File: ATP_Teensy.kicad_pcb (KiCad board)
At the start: 2 copper layers, 73 x 73 mm, 18 parts, among them J1 Screw_Terminal_01x02, U1 BMP388_3966, U2 L7805CV, U3 FT231X_XBee_USB_Adapter, U4 MPU6050, U5 Teensy4.1, U6 GPS

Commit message: Update notes on schematic
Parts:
- 9V PWR: renamed from J1
- renumbered D2 to 5V, D1 to 9V, U1 to BMP, U6 to GPS, U4 to IMU, U2 to REG, U5 to TEENSY4.1, U3 to XBEE_USB
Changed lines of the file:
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@@
     (property "Sheetname" "")
     (attr smd)
-    (fp_text reference "D1" (at 0 -1.68) (layer "F.SilkS")
+    (fp_text reference "9V" (at 0 -1.68) (layer "F.SilkS")
       (effects (font (size 1.2 1.2) (thickness 0.2)))
     )
@@
     (property "Sheetname" "")
     (attr through_hole)
-    (fp_text reference "J1" (at -3.81 0 180) (layer "F.SilkS")
+    (fp_text reference "9V PWR" (at -3.81 0 180) (layer "F.SilkS")
       (effects (font (size 1 1) (thickness 0.15)))
     )
@@
     (property "Sheetname" "")
     (attr through_hole)
-    (fp_text reference "U3" (at 21.495 -39.275 unlocked) (layer "F.SilkS")
+    (fp_text reference "XBEE_USB" (at 21.495 -39.275 unlocked) (layer "F.SilkS")
       (effects (font (size 1 1) (thickness 0.15)))
     )
@@
     (property "Sheetname" "")
     (attr through_hole)
-    (fp_text reference "U4" (at 14.455 1.3075 unlocked) (layer "F.SilkS")
+    (fp_text reference "IMU" (at 14.455 1.3075 unlocked) (layer "F.SilkS")
       (effects (font (size 1 1) (thickness 0.15)))
     )
@@
     (property "Sheetname" "")
     (attr through_hole)
-    (fp_text reference "U2" (at 8.89 -1.27) (layer "F.SilkS")
+    (fp_text reference "REG" (at 8.89 -1.27) (layer "F.SilkS")
       (effects (font (size 1 1) (thickness 0.15)))
     )
@@
     (property "Sheetname" "")
     (attr through_hole)
-    (fp_text reference "U5" (at -26.23 10.16 90) (layer "F.SilkS")
+    (fp_text reference "TEENSY4.1" (at -26.23 10.16 90) (layer "F.SilkS")
       (effects (font (size 1 1) (thickness 0.15)))
     )
@@
     (property "Sheetname" "")
     (attr smd)
-    (fp_text reference "D2" (at 2.54 0 90) (layer "F.SilkS")
+    (fp_text reference "5V" (at 2.54 0 90) (layer "F.SilkS")
       (effects (font (size 1.2 1.2) (thickness 0.2)))
     )
@@
     (property "Sheetname" "")
     (attr through_hole)
-    (fp_text reference "U6" (at 2.54 -1.315 unlocked) (layer "B.SilkS")
+    (fp_text reference "GPS" (at 2.54 -1.315 unlocked) (layer "B.SilkS")
       (effects (font (size 1 1) (thickness 0.15)) (justify mirror))
     )
@@
     (property "Sheetname" "")
     (attr through_hole)
-    (fp_text reference "U1" (at 1.6575 -1.08125 unlocked) (layer "B.SilkS")
+    (fp_text reference "BMP" (at 1.6575 -1.08125 unlocked) (layer "B.SilkS")
       (effects (font (size 1 1) (thickness 0.15)) (justify mirror))
     )

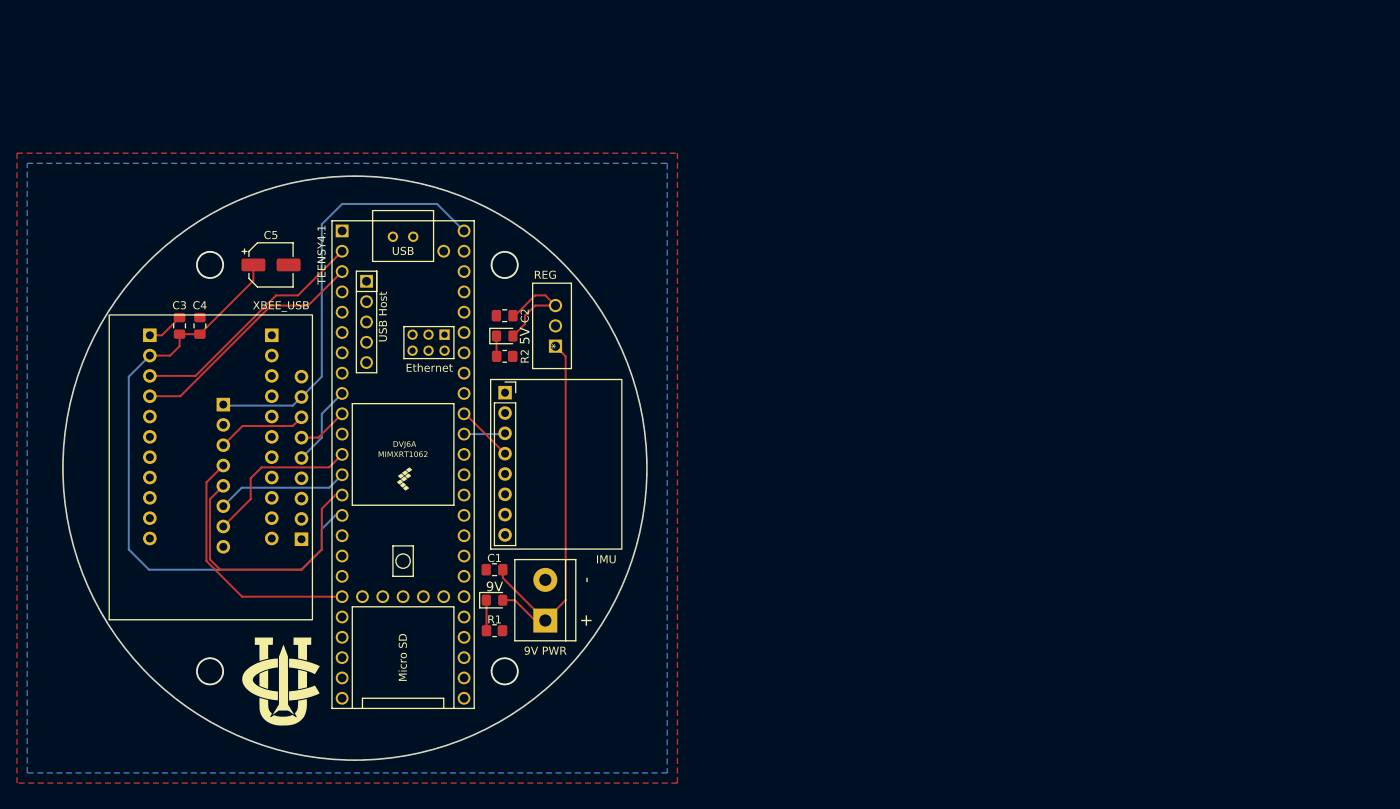
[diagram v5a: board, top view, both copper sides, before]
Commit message: added spi and i2c connections, actual mounting holes, change xbee power input in the schematic
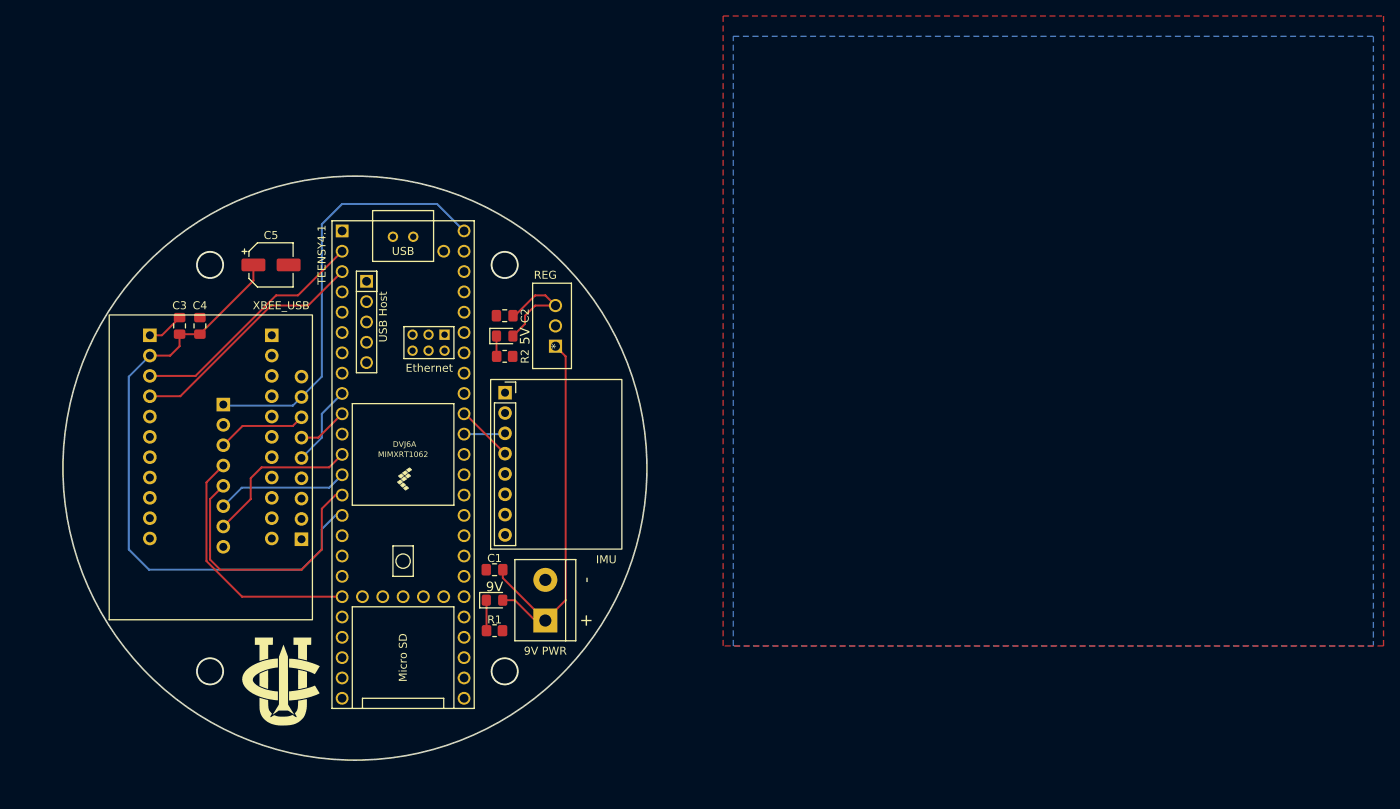
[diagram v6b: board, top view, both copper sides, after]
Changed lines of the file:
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@@
     (polygon
       (pts
-        (xy 193.04 138.43)
-        (xy 110.49 138.43)
-        (xy 110.49 59.69)
-        (xy 193.04 59.69)
+        (xy 281.305 121.285)
+        (xy 198.755 121.285)
+        (xy 198.755 42.545)
+        (xy 281.305 42.545)
       )
     )
@@
     (polygon
       (pts
-        (xy 191.77 137.16)
-        (xy 111.76 137.16)
-        (xy 111.76 60.96)
-        (xy 191.77 60.96)
+        (xy 280.035 121.285)
+        (xy 200.025 121.285)
+        (xy 200.025 45.085)
+        (xy 280.035 45.085)
       )
     )

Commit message: v1.1 Layout done, change direction of reg, added spi and i2c extensions
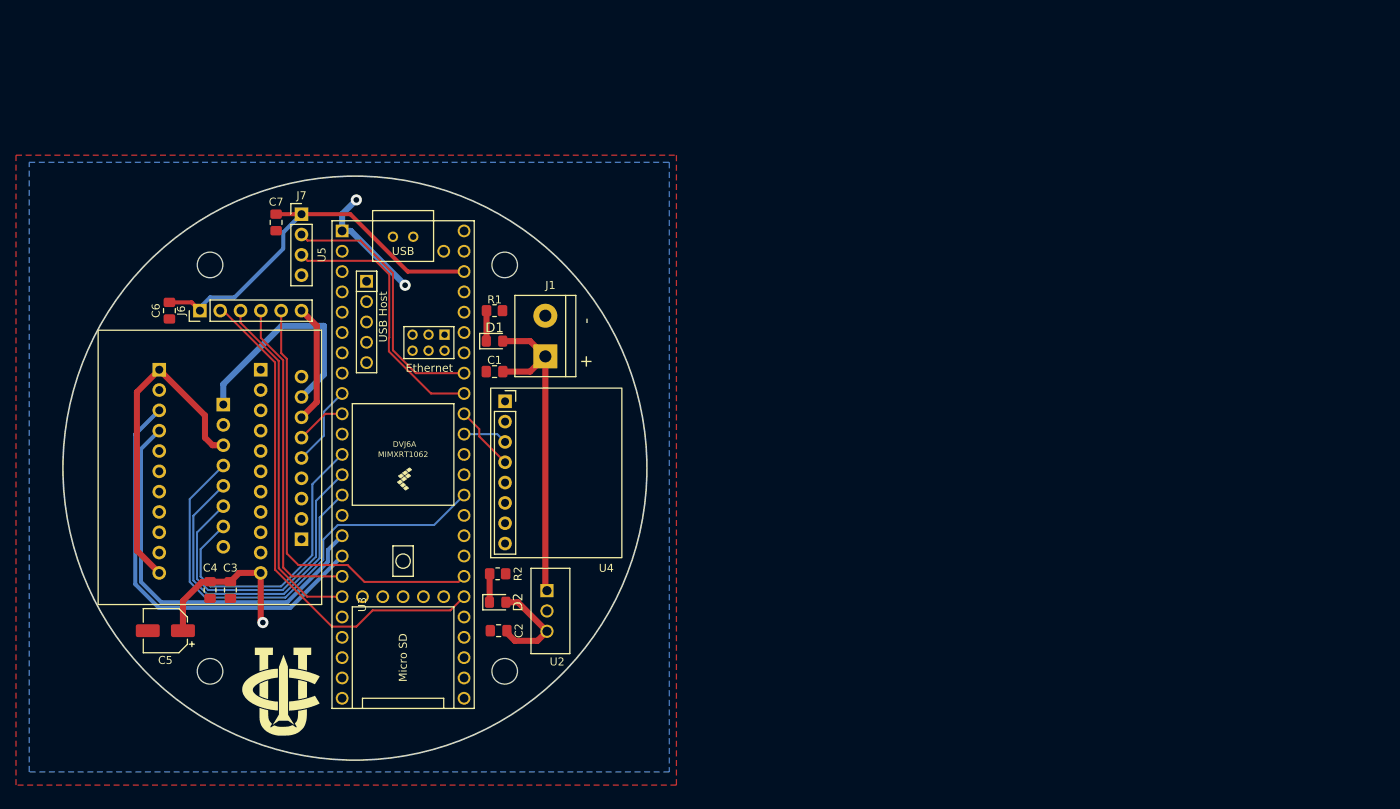
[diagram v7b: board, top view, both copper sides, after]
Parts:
- removed XBEE_USB: FT231X_XBee_USB_Adapter, ATP_Teensy_footprints:XBee_Adapter
- added C6: 1uF, Capacitor_SMD:C_0805_2012Metric_Pad1.18x1.45mm_HandSolder, F.Cu at (129.5, 79.4)
- added C7: 1uF, Capacitor_SMD:C_0805_2012Metric_Pad1.18x1.45mm_HandSolder, F.Cu at (142.9, 68.3)
- added J2: Conn_01x01, MountingHole:MountingHole_3.2mm_M3, F.Cu at (134.6, 124.5)
- added J3: Conn_01x01, MountingHole:MountingHole_3.2mm_M3, F.Cu at (171.4, 124.5)
- added J4: Conn_01x01, MountingHole:MountingHole_3.2mm_M3, F.Cu at (134.6, 73.7)
- added J5: Conn_01x01, MountingHole:MountingHole_3.2mm_M3, F.Cu at (171.4, 73.7)
- added J6: Conn_01x06_Male, Connector_PinHeader_2.54mm:PinHeader_1x06_P2.54mm_Vertical, F.Cu at (133.3, 79.4)
- added J7: Conn_01x04_Male, Connector_PinHeader_2.54mm:PinHeader_1x04_P2.54mm_Vertical, F.Cu at (146.1, 67.3)
- added U3: XBee_SparkfunRegulatedAdapter, ATP_Teensy_footprints:XBee_SparkfunAdapter, F.Cu at (148.6, 116.1)
- J1: renamed from 9V PWR
- moved C5 47.6 mm to (129.0, 119.4), turned to 180 degrees
- moved R1 40.0 mm to (170.2, 79.4)
- moved C2 39.4 mm to (170.7, 119.4)
- moved C3 33.6 mm to (137.2, 114.3), turned to 90 degrees
- moved D2 33.3 mm to (170.6, 115.8)
- moved C4 33.0 mm to (134.6, 114.3), turned to 90 degrees
- moved J1 33.0 mm to (176.5, 85.1)
- moved D1 32.4 mm to (170.2, 83.2)
- moved U2 30.6 mm to (176.7, 114.4), turned to -90 degrees
- moved R2 27.2 mm to (170.6, 112.3)
- moved C1 24.8 mm to (170.2, 87.0)
- moved Ge 1.27 mm to (143.5, 127.0)
- moved Ge 1.27 mm to (144.0, 127.0)
- moved U4 1.07 mm to (169.7, 110.3)
- renumbered 9V to D1, 5V to D2, BMP to U1, REG to U2, IMU to U4, TEENSY4.1 to U5, GPS to U6
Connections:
- C3 pad 2: XBEE_VCC -> +5V
- C4 pad 2: XBEE_VCC -> +5V
- C5 pad 1: XBEE_VCC -> +5V
- U5 pad 15: XBEE_VCC -> unconnected-(U5-Pad15)
- U5 pad 16: unconnected-(U5-Pad16) -> XBEE_DIN
- U5 pad 17: unconnected-(U5-Pad17) -> XBEE_DOUT
- U5 pad 18: unconnected-(U5-Pad18) -> SD_MOSI
- U5 pad 19: BMP_SCK -> SD_SCK
- U5 pad 2: XBEE_DOUT -> unconnected-(U5-Pad2)
- U5 pad 3: XBEE_DIN -> unconnected-(U5-Pad3)
- U5 pad 30: unconnected-(U5-Pad30) -> SD_CS
- U5 pad 31: unconnected-(U5-Pad31) -> SD_MISO
- U5 pad 35: unconnected-(U5-Pad35) -> BMP_SCK
- U5 pad 40: unconnected-(U5-Pad40) -> ECU_SDA
- U5 pad 41: unconnected-(U5-Pad41) -> ECU_SCL
- U5 pad 46: unconnected-(U5-Pad46) -> +3.3V
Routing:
- net XBEE_VCC: track 77.0 -> 0.00 mm
- net SD_CS: track 0.00 -> 63.6 mm
- net GND: track 15.8 -> 72.9 mm, vias 0 -> 2
- net SD_MISO: track 0.00 -> 54.6 mm
- net +3.3V: track 0.00 -> 49.8 mm
- net SD_SCK: track 0.00 -> 43.6 mm
- net SD_MOSI: track 0.00 -> 41.1 mm
- net ECU_SDA: track 0.00 -> 33.2 mm
- net ECU_SCL: track 0.00 -> 33.2 mm
- net BMP_SCK: track 31.6 -> 58.2 mm
- net BMP_SDI: track 16.5 -> 39.2 mm
- net XBEE_DOUT: track 30.5 -> 52.7 mm
- net XBEE_DIN: track 30.5 -> 50.3 mm
- net BMP_CS: track 20.1 -> 37.7 mm
- net +9V: track 50.8 -> 42.9 mm
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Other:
- board text added: "v1.1 {dblquote}Rigel{dblquote} - MAR 2023 - Alexandra Z. J. https://github.com/UCI-Rocket-Project/AFS-PCB"
- board text removed: "v1.0 {dblquote}Rigel{dblquote} - DEC 2022 - Alexandra Z. J. https://github.com/UCI-Rocket-Project/AFS-PCB"

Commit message: Add labels for layout, DRC run, v1.1 Gerber files generated
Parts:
- 9V PWR: renamed from J1
- moved I2C 7.14 mm to (139.2, 69.3), turned to 90 degrees
- moved C7 5.06 mm to (140.2, 72.6), turned to 180 degrees
- moved SPI 0.76 mm to (134.1, 79.4)
- renumbered D2 to 5V, D1 to 9V, U1 to BMP, U6 to GPS, J7 to I2C, U4 to IMU, U2 to REG, J6 to SPI, U5 to TEENSY_4.1, U3 to XBEE
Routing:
- net GND: track 72.9 -> 61.0 mm, vias 2 -> 1
- net ECU_SCL: track 33.2 -> 37.7 mm
- net ECU_SDA: track 33.2 -> 36.3 mm, vias 0 -> 1
- net +3.3V: track 49.8 -> 51.4 mm
- net +9V: track 42.9 -> 41.6 mm
- net +5V: track 63.0 -> 62.3 mm
- net SD_CS: track 63.6 -> 63.0 mm
